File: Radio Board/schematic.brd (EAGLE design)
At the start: 55 x 72.5 mm, 13 parts, among them J1 132134RP

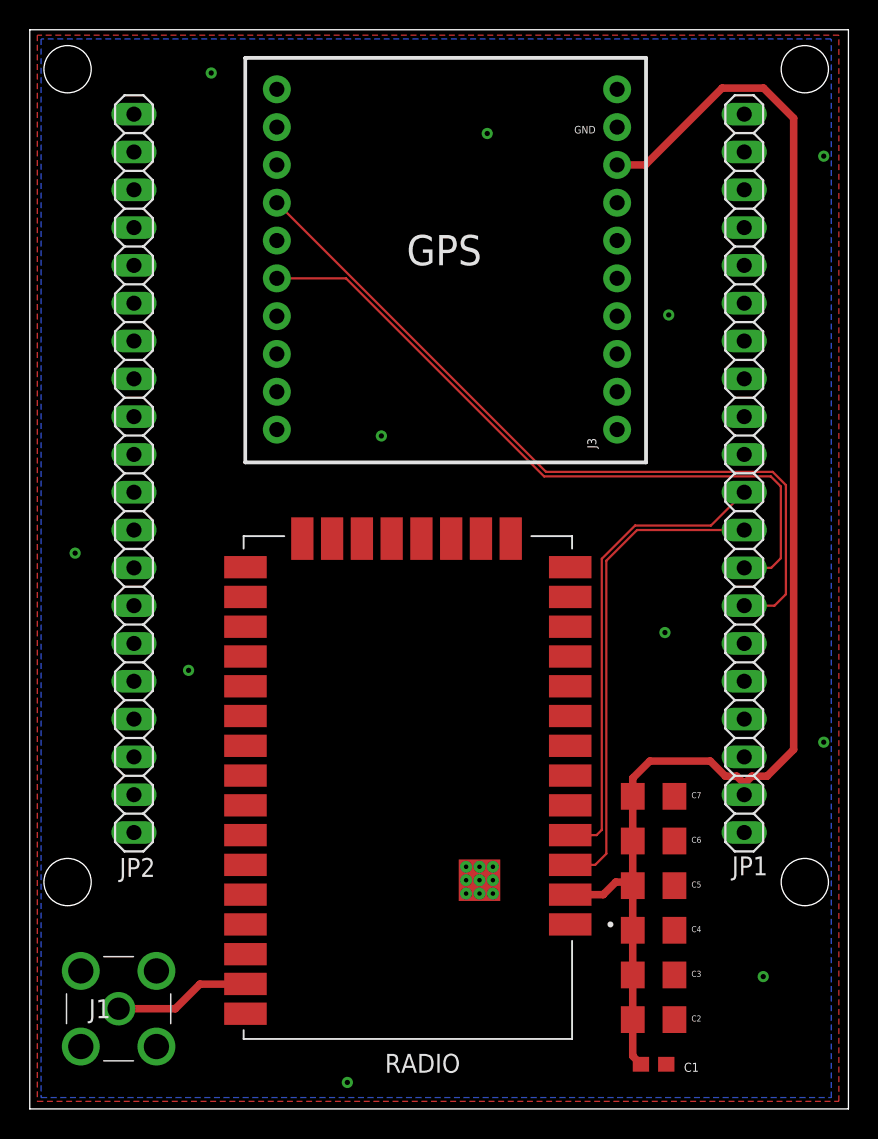
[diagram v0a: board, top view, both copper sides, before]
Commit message: Flipped GPS Module
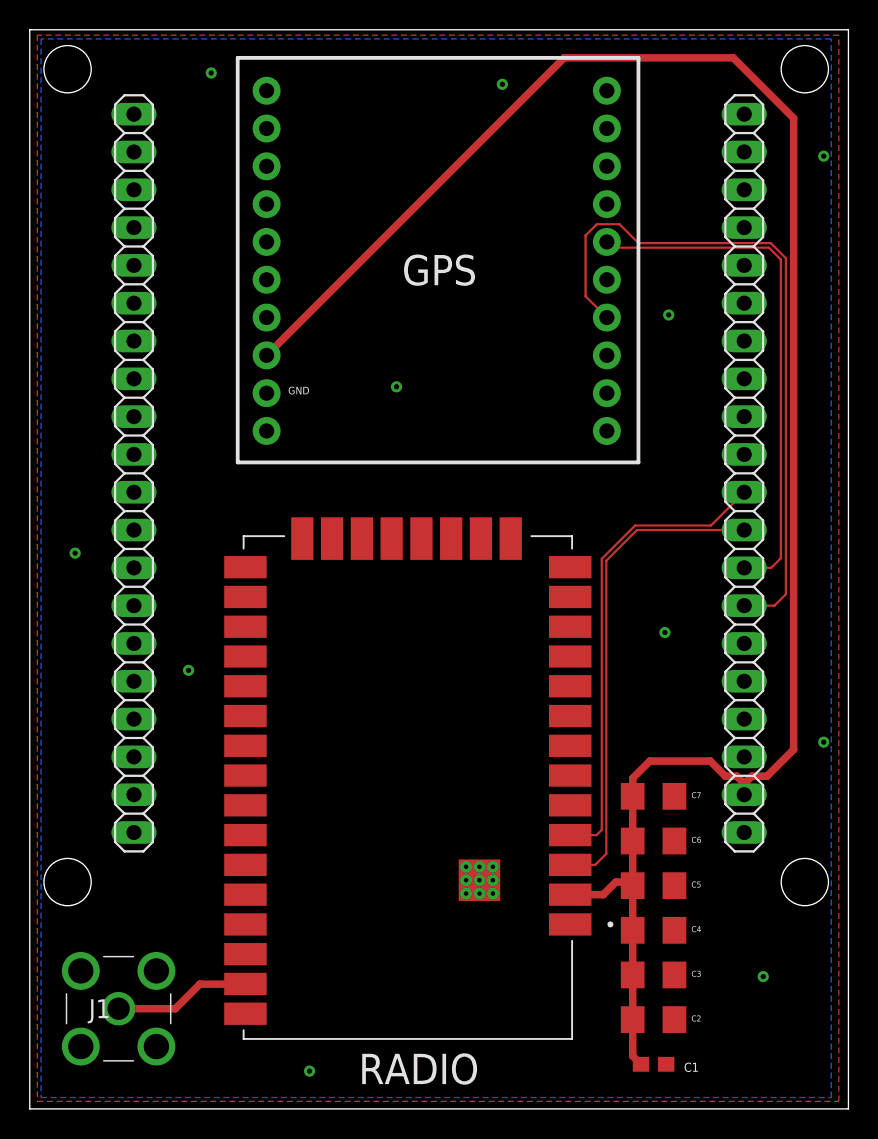
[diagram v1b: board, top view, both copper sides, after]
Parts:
- moved J3 32.8 mm to (15.9, 68.4), turned to 270 degrees
- moved GPS 31.8 mm to (38.8, 68.4), turned to 270 degrees
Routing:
- net 3V3.2: track 111.1 -> 141.6 mm
- net TX1: track 47.2 -> 35.0 mm
- net RX1: track 52.5 -> 46.5 mm
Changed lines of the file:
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@@
 <dimension x1="55" y1="72.7" x2="0" y2="72.7" x3="27.5" y3="77.47" textsize="1.778" layer="1"/>
 <dimension x1="55" y1="0" x2="55" y2="72.5" x3="63.5" y3="36.25" textsize="1.778" layer="1"/>
-<text x="36.576" y="65.532" size="0.508" layer="21">GND</text>
-<wire x1="14.478" y1="70.612" x2="14.478" y2="43.434" width="0.254" layer="21"/>
-<wire x1="14.478" y1="43.434" x2="41.402" y2="43.434" width="0.254" layer="21"/>
-<wire x1="41.402" y1="43.434" x2="41.402" y2="70.612" width="0.254" layer="21"/>
-<wire x1="41.402" y1="70.612" x2="14.478" y2="70.612" width="0.254" layer="21"/>
+<text x="18.796" y="48.514" size="0.508" layer="21" rot="R180">GND</text>
+<wire x1="40.894" y1="43.434" x2="40.894" y2="70.612" width="0.254" layer="21"/>
+<wire x1="40.894" y1="70.612" x2="13.97" y2="70.612" width="0.254" layer="21"/>
+<wire x1="13.97" y1="70.612" x2="13.97" y2="43.434" width="0.254" layer="21"/>
+<wire x1="13.97" y1="43.434" x2="40.894" y2="43.434" width="0.254" layer="21"/>
 </plain>
 <attributes>
@@
 <elements>
 <element name="JP1" library="adafruit" library_urn="urn:adsk.eagle:library:420" package="1X20" package3d_urn="urn:adsk.eagle:package:6240777/1" value="" x="48" y="42.7" smashed="yes" rot="R90">
-<attribute name="NAME" x="49.5782" y="16.9612" size="1.27" layer="25" ratio="10" rot="R180"/>
 <attribute name="VALUE" x="51.175" y="17.3" size="1.27" layer="27" rot="R90"/>
 </element>
 <element name="JP2" library="adafruit" library_urn="urn:adsk.eagle:library:420" package="1X20" package3d_urn="urn:adsk.eagle:package:6240777/1" value="" x="7" y="42.7" smashed="yes" rot="R90">
-<attribute name="NAME" x="8.4302" y="16.8552" size="1.27" layer="25" ratio="10" rot="R180"/>
 <attribute name="VALUE" x="10.175" y="17.3" size="1.27" layer="27" rot="R90"/>
 </element>
-<element name="GPS" library="SparkFun-Connectors" package="1X10_NO_SILK" value="" x="16.6" y="45.64" smashed="yes" rot="R90">
-<attribute name="NAME" x="25.32" y="56.679" size="2.032" layer="25" ratio="20"/>
-<attribute name="VALUE" x="18.632" y="44.37" size="0.6096" layer="27" font="vector" ratio="20" rot="R90"/>
-</element>
-<element name="J3" library="SparkFun-Connectors" package="1X10_NO_SILK" value="" x="39.46" y="45.64" smashed="yes" rot="R90">
-<attribute name="NAME" x="38.063" y="44.37" size="0.6096" layer="25" font="vector" ratio="20" rot="R90"/>
-<attribute name="VALUE" x="41.492" y="44.37" size="0.6096" layer="27" font="vector" ratio="20" rot="R90"/>
+<element name="GPS" library="SparkFun-Connectors" package="1X10_NO_SILK" value="" x="38.772" y="68.406" smashed="yes" rot="R270">
+<attribute name="NAME" x="30.052" y="57.367" size="2.032" layer="25" ratio="20" rot="R180"/>
+<attribute name="VALUE" x="36.74" y="69.676" size="0.6096" layer="27" font="vector" ratio="20" rot="R270"/>
+</element>
+<element name="J3" library="SparkFun-Connectors" package="1X10_NO_SILK" value="" x="15.912" y="68.406" smashed="yes" rot="R270">
+<attribute name="VALUE" x="13.88" y="69.676" size="0.6096" layer="27" font="vector" ratio="20" rot="R270"/>
 </element>
 <element name="C1" library="SparkFun-Capacitors" package="0603" value="100pF" x="41.91" y="3" smashed="yes">
@@
 <attribute name="MF" value="Digi International" x="52.07" y="-19.05" size="1.778" layer="27" rot="R180" display="off"/>
 <attribute name="MP" value="XBP9X-DMRS-001" x="52.07" y="-19.05" size="1.778" layer="27" rot="R180" display="off"/>
-<attribute name="NAME" x="28.924" y="3.7" size="1.27" layer="25" rot="R180"/>
+<attribute name="NAME" x="30.194" y="3.7" size="2.032" layer="25" rot="R180"/>
 <attribute name="PACKAGE" value="Module Digi International" x="52.07" y="-19.05" size="1.778" layer="27" rot="R180" display="off"/>
 <attribute name="PRICE" value="None" x="52.07" y="-19.05" size="1.778" layer="27" rot="R180" display="off"/>
 <attribute name="PURCHASE-URL" value="https://pricing.snapeda.com/search/part/XBP9X-DMRS-001/?ref=eda" x="52.07" y="-19.05" size="1.778" layer="27" rot="R180" display="off"/>
-<attribute name="VALUE" x="32.984" y="40.908" size="1.27" layer="27" rot="R180" align="top-left"/>
 </element>
 <element name="J1" library="132134RP" package="132134RP" value="132134RP" x="5.969" y="6.731" smashed="yes">
@@
 <contactref element="C2" pad="2"/>
 <via x="3.048" y="37.338" extent="1-16" drill="0.35"/>
-<via x="23.622" y="45.212" extent="1-16" drill="0.35"/>
+<via x="31.75" y="68.834" extent="1-16" drill="0.35"/>
 <via x="10.668" y="29.464" extent="1-16" drill="0.35"/>
 <via x="12.192" y="69.596" extent="1-16" drill="0.35"/>
-<via x="30.734" y="65.532" extent="1-16" drill="0.35"/>
+<via x="24.638" y="48.514" extent="1-16" drill="0.35"/>
 <via x="42.926" y="53.34" extent="1-16" drill="0.35"/>
 <via x="53.34" y="64.008" extent="1-16" drill="0.35"/>
@@
 <via x="53.34" y="24.638" extent="1-16" drill="0.35"/>
 <via x="49.276" y="8.89" extent="1-16" drill="0.35"/>
-<via x="21.336" y="1.778" extent="1-16" drill="0.35"/>
+<via x="18.796" y="2.54" extent="1-16" drill="0.35"/>
 <polygon width="0.254" layer="1" isolate="0.635">
 <vertex x="0.508" y="72.136"/>
@@
 <wire x1="40.51" y1="15" x2="40.51" y2="18" width="0.508" layer="1"/>
 <wire x1="40.51" y1="22.222" x2="40.51" y2="18" width="0.508" layer="1"/>
-<wire x1="39.46" y1="63.42" x2="41.355" y2="63.42" width="0.508" layer="1"/>
-<wire x1="41.355" y1="63.42" x2="46.515" y2="68.58" width="0.508" layer="1"/>
-<wire x1="46.515" y1="68.58" x2="49.29888125" y2="68.58" width="0.508" layer="1"/>
-<wire x1="51.319440625" y1="66.559440625" x2="49.29888125" y2="68.58" width="0.508" layer="1"/>
 <wire x1="51.319440625" y1="24.141440625" x2="51.319440625" y2="66.559440625" width="0.508" layer="1"/>
 <wire x1="47.498" y1="22.352" x2="46.736" y2="22.352" width="0.508" layer="1"/>
@@
 <wire x1="41.656" y1="23.368" x2="40.51" y2="22.222" width="0.508" layer="1"/>
 <wire x1="45.72" y1="23.368" x2="41.656" y2="23.368" width="0.508" layer="1"/>
+<wire x1="51.319440625" y1="66.559440625" x2="47.26688125" y2="70.612" width="0.508" layer="1"/>
+<wire x1="35.898" y1="70.612" x2="15.912" y2="50.626" width="0.508" layer="1"/>
+<wire x1="47.26688125" y1="70.612" x2="35.898" y2="70.612" width="0.508" layer="1"/>
 </signal>
 <signal name="LIPO">
@@
 <contactref element="JP1" pad="7"/>
 <contactref element="GPS" pad="7"/>
-<wire x1="16.6" y1="60.88" x2="34.681" y2="42.799" width="0.1524" layer="1"/>
-<wire x1="34.681" y1="42.799" x2="49.911" y2="42.799" width="0.1524" layer="1"/>
-<wire x1="49.911" y1="42.799" x2="50.8" y2="41.91" width="0.1524" layer="1"/>
 <wire x1="50.8" y1="34.578" x2="50.032" y2="33.81" width="0.1524" layer="1"/>
 <wire x1="50.032" y1="33.81" x2="48" y2="33.81" width="0.1524" layer="1"/>
-<wire x1="50.8" y1="41.91" x2="50.8" y2="34.578" width="0.1524" layer="1"/>
+<wire x1="50.8" y1="34.578" x2="50.8" y2="57.15" width="0.1524" layer="1"/>
+<wire x1="40.894" y1="58.166" x2="39.624" y2="59.436" width="0.1524" layer="1"/>
+<wire x1="39.624" y1="59.436" x2="38.1" y2="59.436" width="0.1524" layer="1"/>
+<wire x1="38.1" y1="59.436" x2="37.338" y2="58.674" width="0.1524" layer="1"/>
+<wire x1="37.338" y1="58.674" x2="37.338" y2="54.6" width="0.1524" layer="1"/>
+<wire x1="37.338" y1="54.6" x2="38.772" y2="53.166" width="0.1524" layer="1"/>
+<wire x1="50.8" y1="57.15" x2="49.784" y2="58.166" width="0.1524" layer="1"/>
+<wire x1="49.784" y1="58.166" x2="40.894" y2="58.166" width="0.1524" layer="1"/>
 </signal>
 <signal name="TX1">
 <contactref element="JP1" pad="8"/>
 <contactref element="GPS" pad="5"/>
-<wire x1="16.6" y1="55.8" x2="21.24894375" y2="55.8" width="0.1524" layer="1"/>
-<wire x1="34.55474375" y1="42.4942" x2="49.78474375" y2="42.4942" width="0.1524" layer="1"/>
-<wire x1="49.78474375" y1="42.4942" x2="50.457471875" y2="41.821471875" width="0.1524" layer="1"/>
-<wire x1="21.24894375" y1="55.8" x2="34.55474375" y2="42.4942" width="0.1524" layer="1"/>
-<wire x1="50.457471875" y1="41.821471875" x2="50.457471875" y2="36.995471875" width="0.1524" layer="1"/>
 <wire x1="49.812" y1="36.35" x2="48" y2="36.35" width="0.1524" layer="1"/>
-<wire x1="50.457471875" y1="36.995471875" x2="49.812" y2="36.35" width="0.1524" layer="1"/>
+<wire x1="49.812" y1="36.35" x2="50.457471875" y2="36.995471875" width="0.1524" layer="1"/>
+<wire x1="50.457471875" y1="36.995471875" x2="50.457471875" y2="57.061471875" width="0.1524" layer="1"/>
+<wire x1="50.457471875" y1="57.061471875" x2="49.65774375" y2="57.8612" width="0.1524" layer="1"/>
+<wire x1="39.1568" y1="57.8612" x2="38.772" y2="58.246" width="0.1524" layer="1"/>
+<wire x1="49.65774375" y1="57.8612" x2="39.1568" y2="57.8612" width="0.1524" layer="1"/>
 </signal>
 <signal name="RX2">
